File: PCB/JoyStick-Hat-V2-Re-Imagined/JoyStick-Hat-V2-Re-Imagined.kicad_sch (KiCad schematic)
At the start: 0 parts

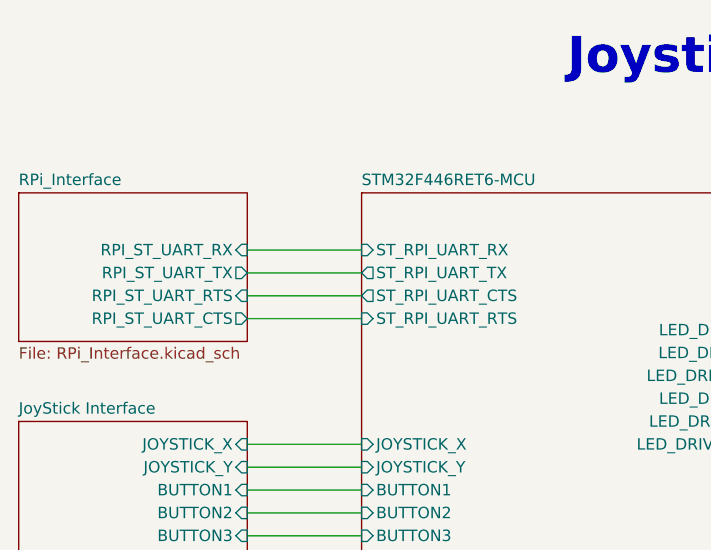
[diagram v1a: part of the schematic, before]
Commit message: RPi Removed
Removed RPi from circuit added 20 pin JTAG schematic and PCB stil WIP
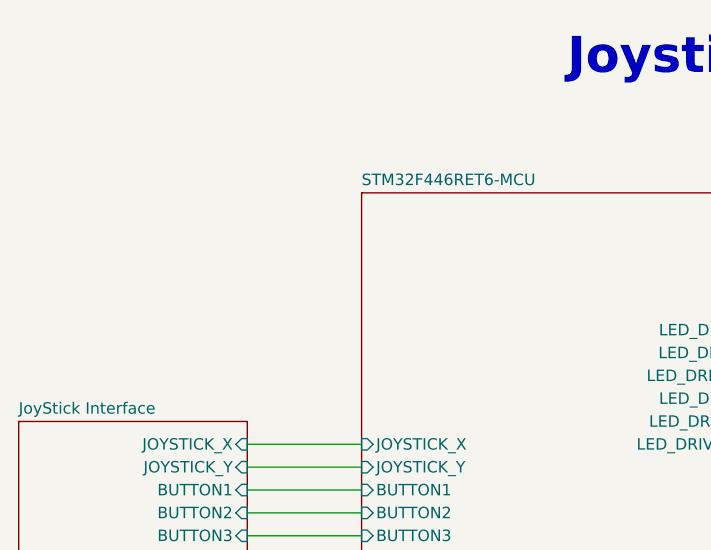
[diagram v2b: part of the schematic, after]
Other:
- removed sheet RPi_Interface
- sheet STM32F446RET6-MCU ports: added none; removed ST_RPI_UART_CTS, ST_RPI_UART_RTS, ST_RPI_UART_RX, ST_RPI_UART_TX
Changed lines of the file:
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@@
-	(wire
-		(pts
-			(xy 101.6 44.45) (xy 114.3 44.45)
-		)
-		(stroke
-			(width 0)
-			(type default)
-		)
-	)
-	(wire
-		(pts
-			(xy 101.6 52.07) (xy 114.3 52.07)
-		)
-		(stroke
-			(width 0)
-			(type default)
-		)
-	)
 	(wire
 		(pts
@@
 	(wire
 		(pts
-			(xy 101.6 46.99) (xy 114.3 46.99)
-		)
-		(stroke
-			(width 0)
-			(type default)
-		)
-	)
-	(wire
-		(pts
 			(xy 101.6 125.73) (xy 114.3 125.73)
 		)
@@
 		(pts
 			(xy 101.6 68.58) (xy 114.3 68.58)
-		)
-		(stroke
-			(width 0)
-			(type default)
-		)
-	)
-	(wire
-		(pts
-			(xy 101.6 49.53) (xy 114.3 49.53)
 		)
 		(stroke
@@
 	)
 	(sheet
-		(at 76.2 38.1)
-		(size 25.4 16.51)
-		(fields_autoplaced yes)
-		(stroke
-			(width 0.1524)
-			(type solid)
-		)
-		(fill
-			(color 0 194 0 1.0000)
-		)
-		(property "Sheetname" "RPi_Interface"
-			(at 76.2 37.3884 0)
-			(effects
-				(font
-					(size 1.27 1.27)
-				)
-				(justify left bottom)
-			)
-		)
-		(property "Sheetfile" "RPi_Interface.kicad_sch"
-			(at 76.2 55.1946 0)
-			(effects
-				(font
-					(size 1.27 1.27)
-				)
-				(justify left top)
-			)
-		)
-		(pin "RPI_ST_UART_RX" input
-			(at 101.6 44.45 0)
-			(effects
-				(font
-					(size 1.27 1.27)
-				)
-				(justify right)
-			)
-		)
-		(pin "RPI_ST_UART_TX" output
-			(at 101.6 46.99 0)
-			(effects
-				(font
-					(size 1.27 1.27)
-				)
-				(justify right)
-			)
-		)
-		(pin "RPI_ST_UART_RTS" input
-			(at 101.6 49.53 0)
-			(effects
-				(font
-					(size 1.27 1.27)
-				)
-				(justify right)
-			)
-		)
-		(pin "RPI_ST_UART_CTS" output
-			(at 101.6 52.07 0)
-			(effects
-				(font
-					(size 1.27 1.27)
-				)
-				(justify right)
-			)
-		)
-		(instances
-			(project "JoyStick-Hat-V2-Re-Imagined"
-				(path "/cf0c81b5-5bdf-47c3-83c0-f6980f515e65"
-					(page "6")
-				)
-			)
-		)
-	)
-	(sheet
 		(at 114.3 152.4)
 		(size 38.1 25.4)
@@
 			)
 		)
-		(pin "ST_RPI_UART_CTS" output
-			(at 114.3 49.53 180)
-			(effects
-				(font
-					(size 1.27 1.27)
-				)
-				(justify left)
-			)
-		)
-		(pin "ST_RPI_UART_RX" input
-			(at 114.3 44.45 180)
-			(effects
-				(font
-					(size 1.27 1.27)
-				)
-				(justify left)
-			)
-		)
-		(pin "ST_RPI_UART_TX" output
-			(at 114.3 46.99 180)
-			(effects
-				(font
-					(size 1.27 1.27)
-				)
-				(justify left)
-			)
-		)
-		(pin "ST_RPI_UART_RTS" input
-			(at 114.3 52.07 180)
-			(effects
-				(font
-					(size 1.27 1.27)
-				)
-				(justify left)
-			)
-		)

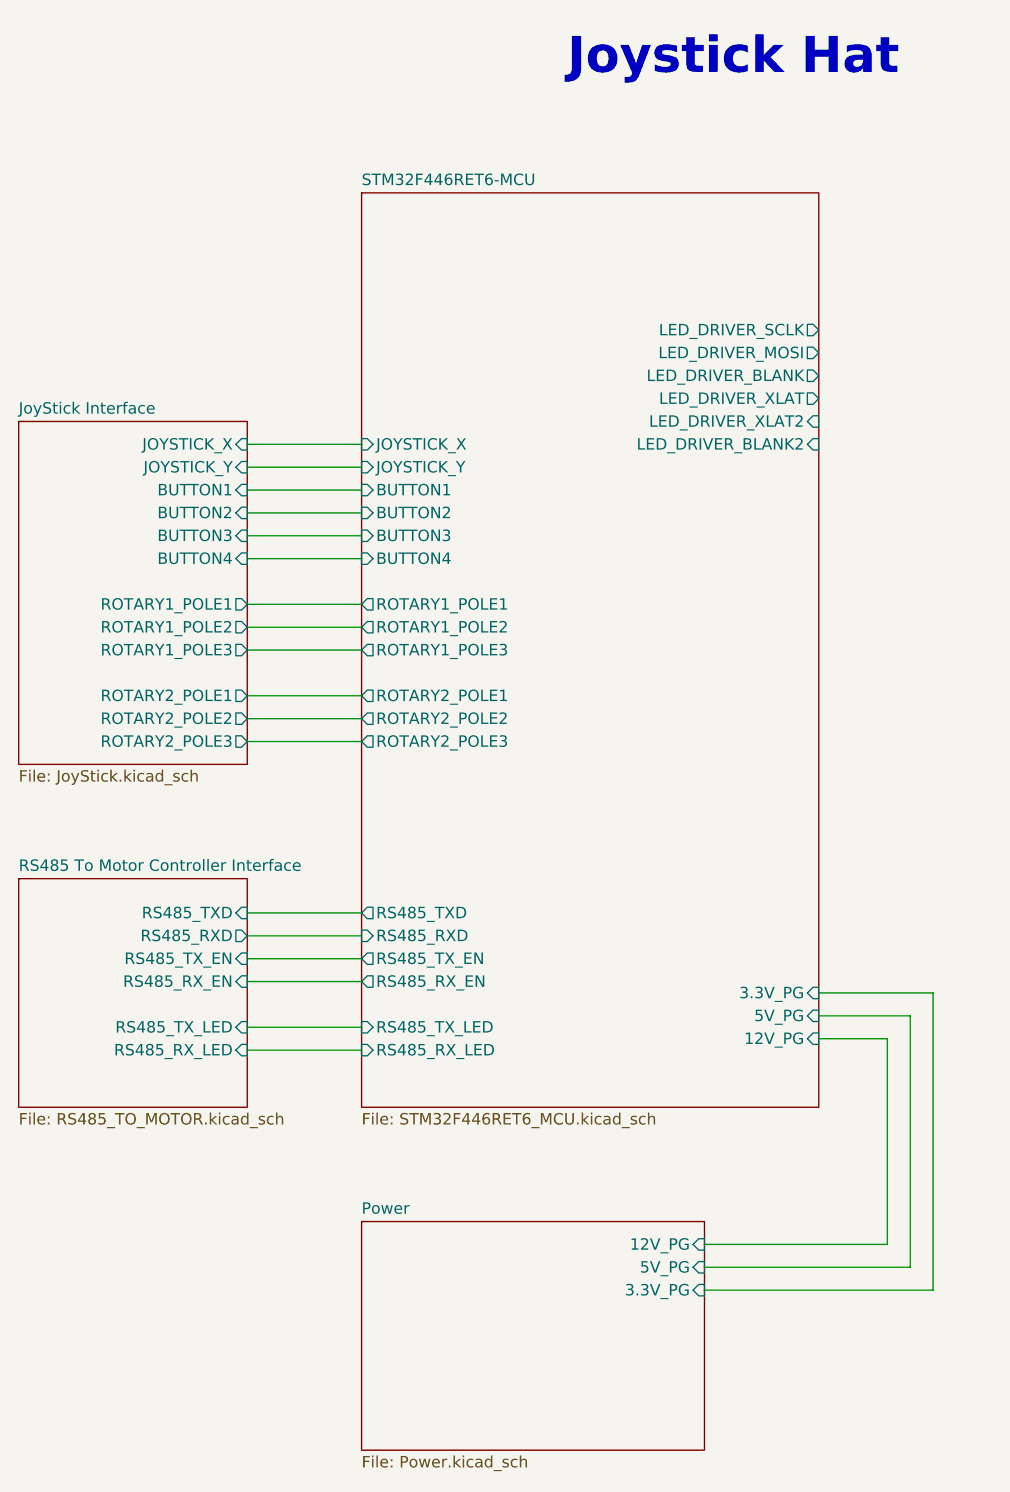
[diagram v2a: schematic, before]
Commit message: Fab Fixes
Fixing for Frabrication, DRC cleared by pending external review subject to change.
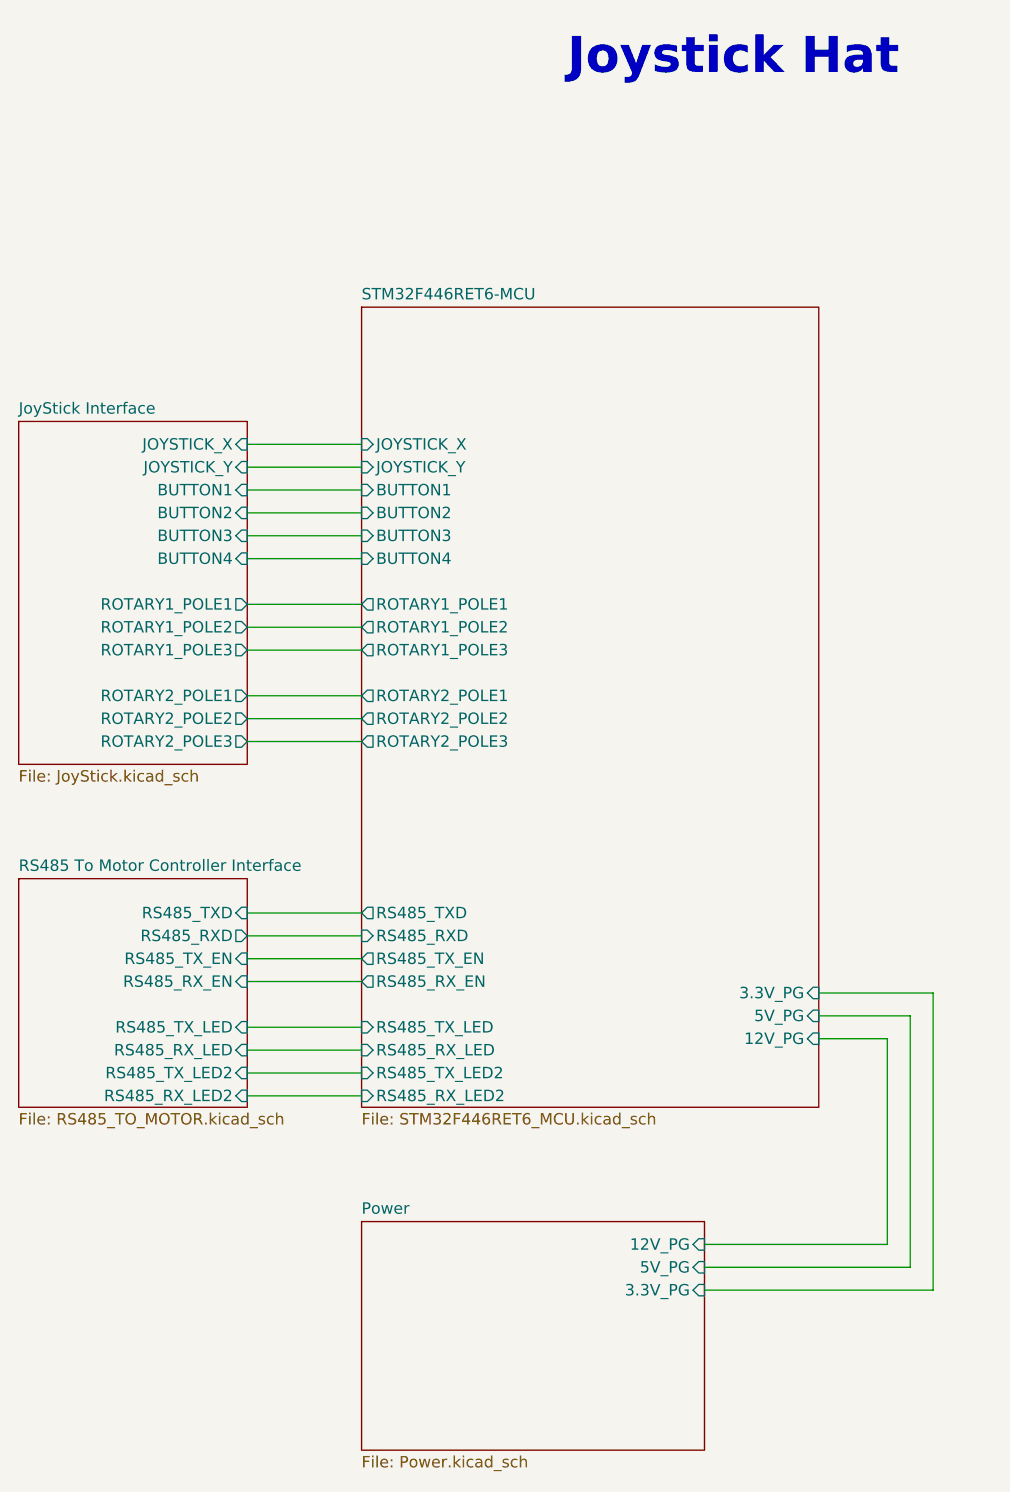
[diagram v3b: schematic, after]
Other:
- sheet RS485 To Motor Controller Interface ports: added RS485_RX_LED2, RS485_TX_LED2; removed none
- sheet STM32F446RET6-MCU ports: added RS485_RX_LED2, RS485_TX_LED2; removed LED_DRIVER_BLANK, LED_DRIVER_BLANK2, LED_DRIVER_MOSI, LED_DRIVER_SCLK, LED_DRIVER_XLAT, LED_DRIVER_XLAT2
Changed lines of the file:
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@@
+	(wire
+		(pts
+			(xy 101.6 138.43) (xy 114.3 138.43)
+		)
+		(stroke
+			(width 0)
+			(type default)
+		)
+	)
 	(wire
 		(pts
@@
 		(pts
 			(xy 165.1 129.54) (xy 175.26 129.54)
+		)
+		(stroke
+			(width 0)
+			(type default)
+		)
+	)
+	(wire
+		(pts
+			(xy 101.6 135.89) (xy 114.3 135.89)
 		)
 		(stroke
@@
 			)
 		)
+		(pin "RS485_TX_LED2" input
+			(at 101.6 135.89 0)
+			(effects
+				(font
+					(size 1.27 1.27)
+				)
+				(justify right)
+			)
+		)
+		(pin "RS485_RX_LED2" input
+			(at 101.6 138.43 0)
+			(effects
+				(font
+					(size 1.27 1.27)
+				)
+				(justify right)
+			)
+		)
 		(instances
 			(project "JoyStick-Hat-V2-Re-Imagined"
@@
 	)
 	(sheet
-		(at 114.3 38.1)
-		(size 50.8 101.6)
+		(at 114.3 50.8)
+		(size 50.8 88.9)
 		(fields_autoplaced yes)
 		(stroke
@@
 		)
 		(property "Sheetname" "STM32F446RET6-MCU"
-			(at 114.3 37.3884 0)
+			(at 114.3 50.0884 0)
 			(effects
 				(font
@@
 			)
 		)
-		(pin "LED_DRIVER_BLANK" output
-			(at 165.1 58.42 0)
-			(effects
-				(font
-					(size 1.27 1.27)
-				)
-				(justify right)
-			)
-		)
-		(pin "LED_DRIVER_SCLK" output
-			(at 165.1 53.34 0)
-			(effects
-				(font
-					(size 1.27 1.27)
-				)
-				(justify right)
-			)
-		)
-		(pin "LED_DRIVER_MOSI" output
-			(at 165.1 55.88 0)
-			(effects
-				(font
-					(size 1.27 1.27)
-				)
-				(justify right)
-			)
-		)
-		(pin "LED_DRIVER_XLAT" output
-			(at 165.1 60.96 0)
-			(effects
-				(font
-					(size 1.27 1.27)
-				)
-				(justify right)
-			)
-		)
 		(pin "BUTTON1" input
 			(at 114.3 71.12 180)
@@
 			)
 		)
-		(pin "LED_DRIVER_BLANK2" input
-			(at 165.1 66.04 0)
-			(effects
-				(font
-					(size 1.27 1.27)
-				)
-				(justify right)
-			)
-		)
-		(pin "LED_DRIVER_XLAT2" input
-			(at 165.1 63.5 0)
-			(effects
-				(font
-					(size 1.27 1.27)
-				)
-				(justify right)
-			)
-		)
 		(pin "RS485_TXD" output
 			(at 114.3 118.11 180)
@@
 			(effects
 				(font
+					(size 1.27 1.27)
+				)
+				(justify left)
+			)
+		)
+		(pin "RS485_RX_LED2" input
+			(at 114.3 138.43 180)
+			(effects
+				(font
+					(size 1.27 1.27)
+				)
+				(justify left)
+			)
+		)
+		(pin "RS485_TX_LED2" input
+			(at 114.3 135.89 180)
+			(effects
+				(font

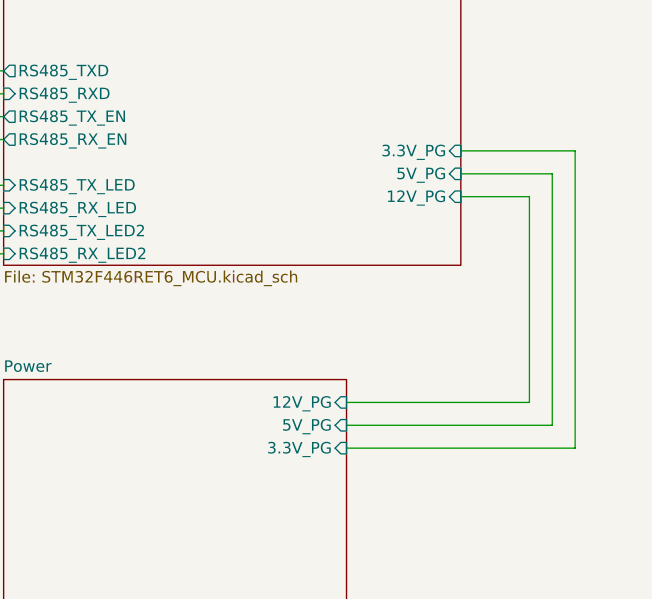
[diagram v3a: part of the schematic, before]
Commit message: Front Page Cleanup
Removed old sheet pins and wires from hierachal page since 12v and 5v are no longer in the system.
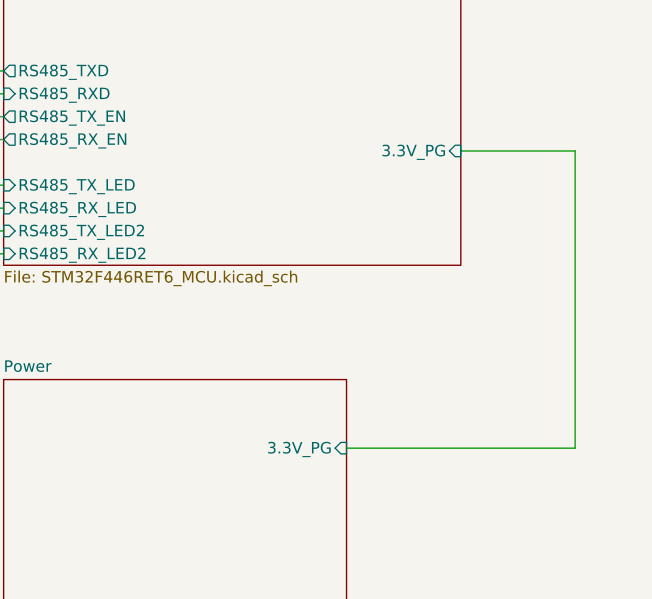
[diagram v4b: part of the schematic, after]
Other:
- sheet Power ports: added none; removed 12V_PG, 5V_PG
- sheet STM32F446RET6-MCU ports: added none; removed 12V_PG, 5V_PG
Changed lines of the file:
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@@
-	(wire
-		(pts
-			(xy 152.4 157.48) (xy 175.26 157.48)
-		)
-		(stroke
-			(width 0)
-			(type default)
-		)
-	)
 	(wire
 		(pts
@@
 	(wire
 		(pts
-			(xy 165.1 129.54) (xy 175.26 129.54)
-		)
-		(stroke
-			(width 0)
-			(type default)
-		)
-	)
-	(wire
-		(pts
 			(xy 101.6 135.89) (xy 114.3 135.89)
 		)
@@
 	(wire
 		(pts
-			(xy 172.72 154.94) (xy 172.72 132.08)
-		)
-		(stroke
-			(width 0)
-			(type default)
-		)
-	)
-	(wire
-		(pts
 			(xy 101.6 73.66) (xy 114.3 73.66)
 		)
@@
 	(wire
 		(pts
-			(xy 172.72 132.08) (xy 165.1 132.08)
-		)
-		(stroke
-			(width 0)
-			(type default)
-		)
-	)
-	(wire
-		(pts
 			(xy 152.4 160.02) (xy 177.8 160.02)
 		)
@@
 		(pts
 			(xy 101.6 130.81) (xy 114.3 130.81)
-		)
-		(stroke
-			(width 0)
-			(type default)
-		)
-	)
-	(wire
-		(pts
-			(xy 175.26 157.48) (xy 175.26 129.54)
-		)
-		(stroke
-			(width 0)
-			(type default)
-		)
-	)
-	(wire
-		(pts
-			(xy 152.4 154.94) (xy 172.72 154.94)
 		)
 		(stroke
@@
 			)
 		)
-		(pin "12V_PG" input
-			(at 152.4 154.94 0)
-			(effects
-				(font
-					(size 1.27 1.27)
-				)
-				(justify right)
-			)
-		)
-		(pin "5V_PG" input
-			(at 152.4 157.48 0)
-			(effects
-				(font
-					(size 1.27 1.27)
-				)
-				(justify right)
-			)
-		)
 		(pin "3.3V_PG" input
 			(at 152.4 160.02 0)
@@
 			)
 		)
-		(pin "12V_PG" input
-			(at 165.1 132.08 0)
-			(effects
-				(font
-					(size 1.27 1.27)
-				)
-				(justify right)
-			)
-		)
 		(pin "3.3V_PG" input
 			(at 165.1 127 0)
 			(effects
 				(font
-					(size 1.27 1.27)
-				)
-				(justify right)
-			)
-		)
-		(pin "5V_PG" input
-			(at 165.1 129.54 0)
-			(effects
-				(font
